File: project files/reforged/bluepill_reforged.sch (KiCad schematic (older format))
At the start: 40 parts, among them J1 USB_C_Receptacle_USB2.0, J2 Left Castellation, J3 STDC14, J4 Right Castellation, SW1 Boot0, SW2 Reset, U1 AMS1117-3.3, U2 STM32F103C8Tx, Y1 8MHz, Y2 32768Hz

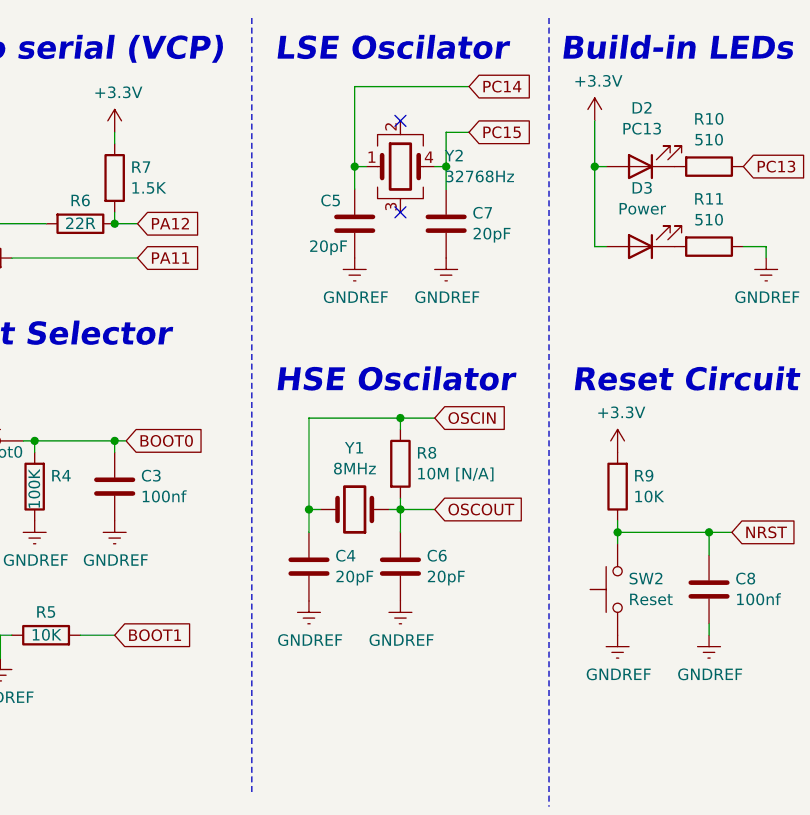
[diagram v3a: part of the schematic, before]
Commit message: replaced crystal with smd
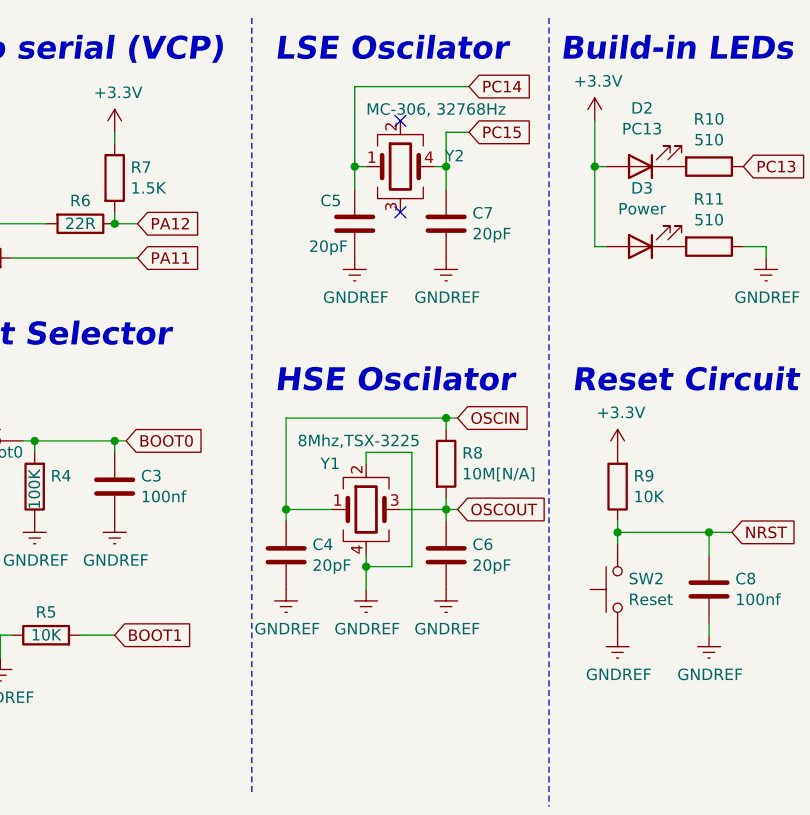
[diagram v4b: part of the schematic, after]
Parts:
- removed Y1: 8MHz, Crystal:Crystal_HC49-4H_Vertical, symbol Device:Crystal
- added Y1: 8Mhz,TSX-3225, Crystal:Crystal_SMD_3225-4Pin_3.2x2.5mm, symbol Device:Crystal_GND24
- R8: value 10M [N/A] -> 10M[N/A]
- Y2: value 32768Hz -> MC-306, 32768Hz
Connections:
- net GNDREF: now also Y1.2, Y1.4
- net OSCIN: now also Y1.1
- net OSCOUT: now also Y1.3
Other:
- moved on the sheet: C4, C6, R8
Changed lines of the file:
@@
 	1    0    0    -1
-$EndComp
-$Comp
-L Device:Crystal Y1
-U 1 1 5DE0EDF5
-P 4650 2650
-F 0 "Y1" H 4650 2382 50  0000 C CNN
-F 1 "8MHz" H 4650 2473 50  0000 C CNN
-F 2 "Crystal:Crystal_HC49-4H_Vertical" H 4650 2650 50  0001 C CNN
-F 3 "~" H 4650 2650 50  0001 C CNN
-	1    4650 2650
-	-1   0    0    1
 $EndComp
 Text Notes 5550 700  0    100  Italic 20
@@
 L Device:C C4
 U 1 1 5DE3364B
-P 4450 2900
-F 0 "C4" H 4565 2946 50  0000 L CNN
-F 1 "20pF" H 4565 2855 50  0000 L CNN
-F 2 "Capacitor_SMD:C_0603_1608Metric_Pad1.05x0.95mm_HandSolder" H 4488 2750 50  0001 C CNN
-F 3 "~" H 4450 2900 50  0001 C CNN
-	1    4450 2900
+P 4350 2850
+F 0 "C4" H 4465 2896 50  0000 L CNN
+F 1 "20pF" H 4465 2805 50  0000 L CNN
+F 2 "Capacitor_SMD:C_0603_1608Metric_Pad1.05x0.95mm_HandSolder" H 4388 2700 50  0001 C CNN
+F 3 "~" H 4350 2850 50  0001 C CNN
+	1    4350 2850
 	1    0    0    -1
 $EndComp
@@
 L Device:C C6
 U 1 1 5DE33802
-P 4850 2900
-F 0 "C6" H 4965 2946 50  0000 L CNN
-F 1 "20pF" H 4965 2855 50  0000 L CNN
-F 2 "Capacitor_SMD:C_0603_1608Metric_Pad1.05x0.95mm_HandSolder" H 4888 2750 50  0001 C CNN
-F 3 "~" H 4850 2900 50  0001 C CNN
-	1    4850 2900
+P 5050 2850
+F 0 "C6" H 5165 2896 50  0000 L CNN
+F 1 "20pF" H 5165 2805 50  0000 L CNN
+F 2 "Capacitor_SMD:C_0603_1608Metric_Pad1.05x0.95mm_HandSolder" H 5088 2700 50  0001 C CNN
+F 3 "~" H 5050 2850 50  0001 C CNN
+	1    5050 2850
 	1    0    0    -1
 $EndComp
@@
 Wire Wire Line
 	5050 1150 5050 1250
-Wire Wire Line
-	4450 2750 4450 2650
-Wire Wire Line
-	4500 2650 4450 2650
-Wire Wire Line
-	4800 2650 4850 2650
-Wire Wire Line
-	4850 2650 4850 2750
-Connection ~ 4850 2650
-Wire Wire Line
-	4850 2650 5000 2650
 $Comp
 L Device:R R3
@@
 L power:GNDREF #PWR016
 U 1 1 5DE9A513
-P 4450 3050
-F 0 "#PWR016" H 4450 2800 50  0001 C CNN
-F 1 "GNDREF" H 4455 2877 50  0000 C CNN
-F 2 "" H 4450 3050 50  0001 C CNN
-F 3 "" H 4450 3050 50  0001 C CNN
-	1    4450 3050
+P 4350 3000
+F 0 "#PWR016" H 4350 2750 50  0001 C CNN
+F 1 "GNDREF" H 4355 2827 50  0000 C CNN
+F 2 "" H 4350 3000 50  0001 C CNN
+F 3 "" H 4350 3000 50  0001 C CNN
+	1    4350 3000
 	1    0    0    -1
 $EndComp
@@
 L power:GNDREF #PWR018
 U 1 1 5DE9A892
-P 4850 3050
-F 0 "#PWR018" H 4850 2800 50  0001 C CNN
-F 1 "GNDREF" H 4855 2877 50  0000 C CNN
-F 2 "" H 4850 3050 50  0001 C CNN
-F 3 "" H 4850 3050 50  0001 C CNN
-	1    4850 3050
+P 5050 3000
+F 0 "#PWR018" H 5050 2750 50  0001 C CNN
+F 1 "GNDREF" H 5055 2827 50  0000 C CNN
+F 2 "" H 5050 3000 50  0001 C CNN
+F 3 "" H 5050 3000 50  0001 C CNN
+	1    5050 3000
 	1    0    0    -1
 $EndComp
@@
 P 4850 1150
 F 0 "Y2" H 5044 1196 50  0000 L CNN
-F 1 "32768Hz" H 5044 1105 50  0000 L CNN
+F 1 "MC-306, 32768Hz" H 4700 1400 50  0000 L CNN
 F 2 "Crystal:Crystal_SMD_SeikoEpson_MC306-4Pin_8.0x3.2mm" H 4850 1150 50  0001 C CNN
 F 3 "~" H 4850 1150 50  0001 C CNN
@@
 Text GLabel 7250 2550 0    50   Input ~ 0
 BOOT1
-Connection ~ 4450 2650
 Wire Wire Line
 	4650 1150 4650 800
@@
 Text GLabel 7250 1250 0    50   Input ~ 0
 NRST
-Text GLabel 5000 2250 2    50   Input ~ 0
+Text GLabel 5100 2250 2    50   Input ~ 0
 OSCIN
-Text GLabel 5000 2650 2    50   Input ~ 0
+Text GLabel 5100 2650 2    50   Input ~ 0
 OSCOUT
 Text GLabel 7250 1650 0    50   Input ~ 0
@@
 L Device:R R8
 U 1 1 5E527ACB
-P 4850 2450
-F 0 "R8" H 4920 2496 50  0000 L CNN
-F 1 "10M [N/A]" H 4920 2405 50  0000 L CNN
-F 2 "Resistor_SMD:R_0603_1608Metric_Pad1.05x0.95mm_HandSolder" V 4780 2450 50  0001 C CNN
-F 3 "~" H 4850 2450 50  0001 C CNN
-	1    4850 2450
-	1    0    0    -1
-$EndComp
-Wire Wire Line
-	5000 2250 4850 2250
-Wire Wire Line
-	4450 2250 4450 2650
-Wire Wire Line
-	4850 2300 4850 2250
-Connection ~ 4850 2250
-Wire Wire Line
-	4850 2250 4450 2250
-Wire Wire Line
-	4850 2600 4850 2650
+P 5050 2450
+F 0 "R8" H 5120 2496 50  0000 L CNN
+F 1 "10M[N/A]" H 5120 2405 50  0000 L CNN
+F 2 "Resistor_SMD:R_0603_1608Metric_Pad1.05x0.95mm_HandSolder" V 4980 2450 50  0001 C CNN
+F 3 "~" H 5050 2450 50  0001 C CNN
+	1    5050 2450
+	1    0    0    -1
+$EndComp
 Text GLabel 8550 2350 2    50   Input ~ 0
 PA0
@@
 Wire Wire Line
 	1650 1050 1600 1050
+$Comp
+L Device:Crystal_GND24 Y1
+U 1 1 5E68257B
+P 4700 2650
+F 0 "Y1" H 4500 2850 50  0000 L CNN
+F 1 "8Mhz,TSX-3225" H 4400 2950 50  0000 L CNN
+F 2 "Crystal:Crystal_SMD_3225-4Pin_3.2x2.5mm" H 4700 2650 50  0001 C CNN
+F 3 "~" H 4700 2650 50  0001 C CNN
+	1    4700 2650
+	1    0    0    -1
+$EndComp
+$Comp
+L power:GNDREF #PWR0101
+U 1 1 5E6B7D98
+P 4700 3000
+F 0 "#PWR0101" H 4700 2750 50  0001 C CNN
+F 1 "GNDREF" H 4705 2827 50  0000 C CNN
+F 2 "" H 4700 3000 50  0001 C CNN
+F 3 "" H 4700 3000 50  0001 C CNN
+	1    4700 3000
+	1    0    0    -1
+$EndComp
+Wire Wire Line
+	4550 2650 4350 2650
+Wire Wire Line
+	4350 2650 4350 2250
+Wire Wire Line
+	4850 2650 5050 2650
+Wire Wire Line
+	4350 2250 5050 2250
+Wire Wire Line
+	5050 2300 5050 2250
+Connection ~ 5050 2250
+Wire Wire Line
+	5050 2250 5100 2250
+Wire Wire Line
+	5050 2600 5050 2650
+Connection ~ 5050 2650
+Wire Wire Line
+	5050 2650 5100 2650
+Wire Wire Line
+	4700 3000 4700 2900
+Wire Wire Line
+	5050 2700 5050 2650
+Wire Wire Line
+	4350 2700 4350 2650
+Connection ~ 4350 2650
+Wire Wire Line
+	4700 2450 4700 2400
+Wire Wire Line
+	4700 2400 4900 2400
+Wire Wire Line
+	4900 2400 4900 2900
+Wire Wire Line
+	4900 2900 4700 2900
+Connection ~ 4700 2900
+Wire Wire Line
+	4700 2900 4700 2850
 $EndSCHEMATC

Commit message: Update bluepill_reforged.sch
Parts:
- D2, D3: footprint LED_SMD:LED_0805_2012Metric_Castellated -> LED_SMD:LED_0603_1608Metric_Castellated
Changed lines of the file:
@@
 F 0 "D3" H 5893 1245 50  0000 C CNN
 F 1 "Power" H 5893 1336 50  0000 C CNN
-F 2 "LED_SMD:LED_0805_2012Metric_Castellated" H 5900 1500 50  0001 C CNN
+F 2 "LED_SMD:LED_0603_1608Metric_Castellated" H 5900 1500 50  0001 C CNN
 F 3 "~" H 5900 1500 50  0001 C CNN
 	1    5900 1500
@@
 F 0 "D2" H 5893 895 50  0000 C CNN
 F 1 "PC13" H 5893 986 50  0000 C CNN
-F 2 "LED_SMD:LED_0805_2012Metric_Castellated" H 5900 1150 50  0001 C CNN
+F 2 "LED_SMD:LED_0603_1608Metric_Castellated" H 5900 1150 50  0001 C CNN
 F 3 "~" H 5900 1150 50  0001 C CNN
 	1    5900 1150

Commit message: re-arrangements
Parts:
- C1, C2: footprint Capacitor_Tantalum_SMD:CP_EIA-6032-20_AVX-F_Pad2.25x2.35mm_HandSolder -> Capacitor_Tantalum_SMD:CP_EIA-3528-12_Kemet-T
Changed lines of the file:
@@
 F 0 "C1" H 1018 6296 50  0000 L CNN
 F 1 "0.1-10 uF" H 1018 6205 50  0000 L CNN
-F 2 "Capacitor_Tantalum_SMD:CP_EIA-6032-20_AVX-F_Pad2.25x2.35mm_HandSolder" H 938 6100 50  0001 C CNN
+F 2 "Capacitor_Tantalum_SMD:CP_EIA-3528-12_Kemet-T" H 938 6100 50  0001 C CNN
 F 3 "~" H 900 6250 50  0001 C CNN
 	1    900  6250
@@
 F 0 "C2" H 1818 6296 50  0000 L CNN
 F 1 "47-1000 uF" H 1818 6205 50  0000 L CNN
-F 2 "Capacitor_Tantalum_SMD:CP_EIA-6032-20_AVX-F_Pad2.25x2.35mm_HandSolder" H 1738 6100 50  0001 C CNN
+F 2 "Capacitor_Tantalum_SMD:CP_EIA-3528-12_Kemet-T" H 1738 6100 50  0001 C CNN
 F 3 "~" H 1700 6250 50  0001 C CNN
 	1    1700 6250

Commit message: updates
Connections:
- net +3V3: no longer R7.1
- net VBUS: now also R7.1
- net GNDREF renamed GNDD

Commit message: rearranged
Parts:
- added J5: STDC14, Connector_PinHeader_1.27mm:PinHeader_2x07_P1.27mm_Vertical, symbol Connector_Generic:Conn_02x07_Odd_Even
- Y1: value 8Mhz,TSX-3225 -> 8MHz; footprint Crystal:Crystal_SMD_3225-4Pin_3.2x2.5mm -> Crystal:Crystal_SMD_TXC_7M-4Pin_3.2x2.5mm
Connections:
- net +3V3: now also J5.3 (Pin_3)
- net GNDD: now also J5.11 (Pin_11), J5.5 (Pin_5), J5.7 (Pin_7)
- net NRST: now also J5.12 (Pin_12)
- net PA10: now also J5.13 (Pin_13)
- net PA13: now also J5.4 (Pin_4)
- net PA14: now also J5.6 (Pin_6)
- net PA9: now also J5.14 (Pin_14)
- net PB3: now also J5.8 (Pin_8)
- no-connect marks 8 -> 12
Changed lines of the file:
@@
-	1    0    0    -1
-$EndComp
-$Comp
-L Regulator_Linear:AMS1117-3.3 U1
-U 1 1 5E0AB632
-P 1300 5950
-F 0 "U1" H 1300 6192 50  0000 C CNN
-F 1 "AMS1117-3.3" H 1300 6101 50  0000 C CNN
-F 2 "Package_TO_SOT_SMD:SOT-223-3_TabPin2" H 1300 6150 50  0001 C CNN
-F 3 "http://www.advanced-monolithic.com/pdf/ds1117.pdf" H 1400 5700 50  0001 C CNN
-	1    1300 5950
 	1    0    0    -1
 $EndComp
@@
 PB12
 $Comp
-L Connector_Generic:Conn_01x20 J2
-U 1 1 5DEFD8E5
-P 9700 5350
-F 0 "J2" H 9700 4150 50  0000 C CNN
-F 1 "Left Castellation" H 9700 4200 50  0001 C CNN
-F 2 "Connector_PinHeader_2.54mm:PinHeader_1x20_P2.54mm_Vertical" H 9700 5350 50  0001 C CNN
-F 3 "~" H 9700 5350 50  0001 C CNN
-	1    9700 5350
-	-1   0    0    1
-$EndComp
-$Comp
 L power:+5V #PWR035
 U 1 1 5E5BBA7B
@@
 	10200 6050 10200 5950
 $Comp
-L power:+3.3V #PWR032
-U 1 1 5E5CAD12
-P 9450 6250
-F 0 "#PWR032" H 9450 6100 50  0001 C CNN
-F 1 "+3.3V" H 9465 6423 50  0000 C CNN
-F 2 "" H 9450 6250 50  0001 C CNN
-F 3 "" H 9450 6250 50  0001 C CNN
-	1    9450 6250
-	1    0    0    -1
-$EndComp
-Wire Wire Line
-	9900 6250 10000 6250
-$Comp
 L power:+3.3V #PWR039
 U 1 1 5E5D19A3
@@
 Wire Wire Line
 	10550 4350 10550 4250
-Wire Wire Line
-	10000 6250 10000 6350
-Wire Wire Line
-	10000 6350 9450 6350
-Wire Wire Line
-	9450 6250 9450 6350
 Text GLabel 9250 2600 0    50   Input ~ 0
 SWO
@@
 Wire Wire Line
 	1650 1050 1600 1050
-$Comp
-L Device:Crystal_GND24 Y1
-U 1 1 5E68257B
-P 4700 2650
-F 0 "Y1" H 4500 2850 50  0000 L CNN
-F 1 "8Mhz,TSX-3225" H 4400 2950 50  0000 L CNN
-F 2 "Crystal:Crystal_SMD_3225-4Pin_3.2x2.5mm" H 4700 2650 50  0001 C CNN
-F 3 "~" H 4700 2650 50  0001 C CNN
-	1    4700 2650
-	1    0    0    -1
-$EndComp
 Wire Wire Line
 	4550 2650 4350 2650
@@
 	5050 2650 5100 2650
 Wire Wire Line
-	4700 3000 4700 2900
-Wire Wire Line
 	5050 2700 5050 2650
 Wire Wire Line
 	4350 2700 4350 2650
 Connection ~ 4350 2650
-Wire Wire Line
-	4700 2450 4700 2400
-Wire Wire Line
-	4700 2400 4900 2400
-Wire Wire Line
-	4900 2400 4900 2900
-Wire Wire Line
-	4900 2900 4700 2900
-Connection ~ 4700 2900
-Wire Wire Line
-	4700 2900 4700 2850
 $Comp
 L power:VBUS #PWR0102
@@
 $EndComp
 $Comp
-L power:GNDD #PWR0110
-U 1 1 5E9062A7
-P 4700 3000
-F 0 "#PWR0110" H 4700 2750 50  0001 C CNN
-F 1 "GNDD" H 4704 2845 50  0000 C CNN
-F 2 "" H 4700 3000 50  0001 C CNN
-F 3 "" H 4700 3000 50  0001 C CNN
-	1    4700 3000
-	1    0    0    -1
-$EndComp
-$Comp
 L power:GNDD #PWR0111
 U 1 1 5E9064C7
@@
 Wire Wire Line
 	10200 6150 10200 6300
+$Comp
+L Connector_Generic:Conn_02x07_Odd_Even J5
+U 1 1 5F2A0D58
+P 6000 7200
+F 0 "J5" H 6050 7717 50  0000 C CNN
+F 1 "STDC14" H 6050 7626 50  0000 C CNN
+F 2 "Connector_PinHeader_1.27mm:PinHeader_2x07_P1.27mm_Vertical" H 6000 7200 50  0001 C CNN
+F 3 "~" H 6000 7200 50  0001 C CNN
+	1    6000 7200
+	1    0    0    -1
+$EndComp
+NoConn ~ 5800 6900
+NoConn ~ 6300 6900
+Text GLabel 6300 7100 2    50   Input ~ 0
+SWCLK
+Text GLabel 6300 7400 2    50   Input ~ 0
+NRST
+Text GLabel 6300 7000 2    50   Input ~ 0
+SWDIO
+$Comp
+L power:+3.3V #PWR0110
+U 1 1 5F2A0D63
+P 5400 6800
+F 0 "#PWR0110" H 5400 6650 50  0001 C CNN
+F 1 "+3.3V" H 5415 6928 50  0000 L CNN
+F 2 "" H 5400 6800 50  0001 C CNN
+F 3 "" H 5400 6800 50  0001 C CNN
+	1    5400 6800
+	1    0    0    -1
+$EndComp
+Wire Wire Line
+	5800 7000 5400 7000
+Wire Wire Line
+	5400 7000 5400 6800
+Text GLabel 6300 7200 2    50   Input ~ 0
+SWO
+NoConn ~ 6300 7300
+NoConn ~ 5800 7300
+Wire Wire Line
+	5800 7100 5700 7100
+Wire Wire Line
+	5700 7100 5700 7200
+Wire Wire Line
+	5700 7200 5800 7200
+Wire Wire Line
+	5800 7400 5700 7400
+Wire Wire Line
+	5700 7400 5700 7200
+Connection ~ 5700 7200
+Wire Wire Line
+	5700 7100 5400 7100
+Wire Wire Line
+	5400 7100 5400 7200
+Connection ~ 5700 7100
+Text GLabel 6300 7500 2    50   Output ~ 0
+TX
+Text GLabel 5800 7500 0    50   Input ~ 0
+RX
+$Comp
+L power:GNDD #PWR0129
+U 1 1 5F2A0D79
+P 5400 7200
+F 0 "#PWR0129" H 5400 6950 50  0001 C CNN
+F 1 "GNDD" H 5404 7045 50  0000 C CNN
+F 2 "" H 5400 7200 50  0001 C CNN
+F 3 "" H 5400 7200 50  0001 C CNN
+	1    5400 7200
+	1    0    0    -1
+$EndComp
+$Comp
+L Device:Crystal_GND24 Y1
+U 1 1 5F2F82E0
+P 4700 2650
+F 0 "Y1" H 4400 2950 50  0000 L CNN
+F 1 "8MHz" H 4400 2850 50  0000 L CNN
+F 2 "Crystal:Crystal_SMD_TXC_7M-4Pin_3.2x2.5mm" H 4700 2650 50  0001 C CNN
+F 3 "~" H 4700 2650 50  0001 C CNN
+	1    4700 2650
+	1    0    0    -1
+$EndComp
+Wire Wire Line
+	4700 2850 4700 2900
+Wire Wire Line
+	4700 2900 4900 2900
+Wire Wire Line
+	4900 2900 4900 2400
+Wire Wire Line
+	4900 2400 4700 2400
+Wire Wire Line
+	4700 2400 4700 2450
+Connection ~ 4700 2900
+$Comp
+L power:GNDD #PWR0130
+U 1 1 5F3045BA
+P 4700 3000
+F 0 "#PWR0130" H 4700 2750 50  0001 C CNN
+F 1 "GNDD" H 4704 2845 50  0000 C CNN
+F 2 "" H 4700 3000 50  0001 C CNN
+F 3 "" H 4700 3000 50  0001 C CNN
+	1    4700 3000
+	1    0    0    -1
+$EndComp
+Wire Wire Line
+	4700 2900 4700 3000
+Wire Wire Line
+	9900 6250 10000 6250
+Wire Wire Line
+	10000 6250 10000 6350
+$Comp
+L Connector_Generic:Conn_01x20 J2
+U 1 1 5DEFD8E5
+P 9700 5350
+F 0 "J2" H 9700 4150 50  0000 C CNN
+F 1 "Left Castellation" H 9700 4200 50  0001 C CNN
+F 2 "Connector_PinHeader_2.54mm:PinHeader_1x20_P2.54mm_Vertical" H 9700 5350 50  0001 C CNN
+F 3 "~" H 9700 5350 50  0001 C CNN
+	1    9700 5350
+	-1   0    0    1
+$EndComp
+Wire Wire Line
+	9450 6250 9450 6350
+Wire Wire Line
+	10000 6350 9450 6350
+$Comp
+L power:+3.3V #PWR032
+U 1 1 5E5CAD12
+P 9450 6250
+F 0 "#PWR032" H 9450 6100 50  0001 C CNN
+F 1 "+3.3V" H 9465 6423 50  0000 C CNN
+F 2 "" H 9450 6250 50  0001 C CNN
+F 3 "" H 9450 6250 50  0001 C CNN
+	1    9450 6250
+	1    0    0    -1
+$EndComp
+$Comp
+L Regulator_Linear:AMS1117-3.3 U1
+U 1 1 5F294175
+P 1300 5950
+F 0 "U1" H 1300 6192 50  0000 C CNN
+F 1 "AMS1117-3.3" H 1300 6101 50  0000 C CNN
+F 2 "Package_TO_SOT_SMD:SOT-223-3_TabPin2" H 1300 6150 50  0001 C CNN
+F 3 "http://www.advanced-monolithic.com/pdf/ds1117.pdf" H 1400 5700 50  0001 C CNN
+	1    1300 5950
+	1    0    0    -1
+$EndComp
 $EndSCHEMATC
